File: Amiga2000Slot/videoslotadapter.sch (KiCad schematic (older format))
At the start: 20 parts, among them U1 74LVC86, U2 74LVC574, U3 74LVC574, U4 TLV74333PDBVR, U5 74LVC86

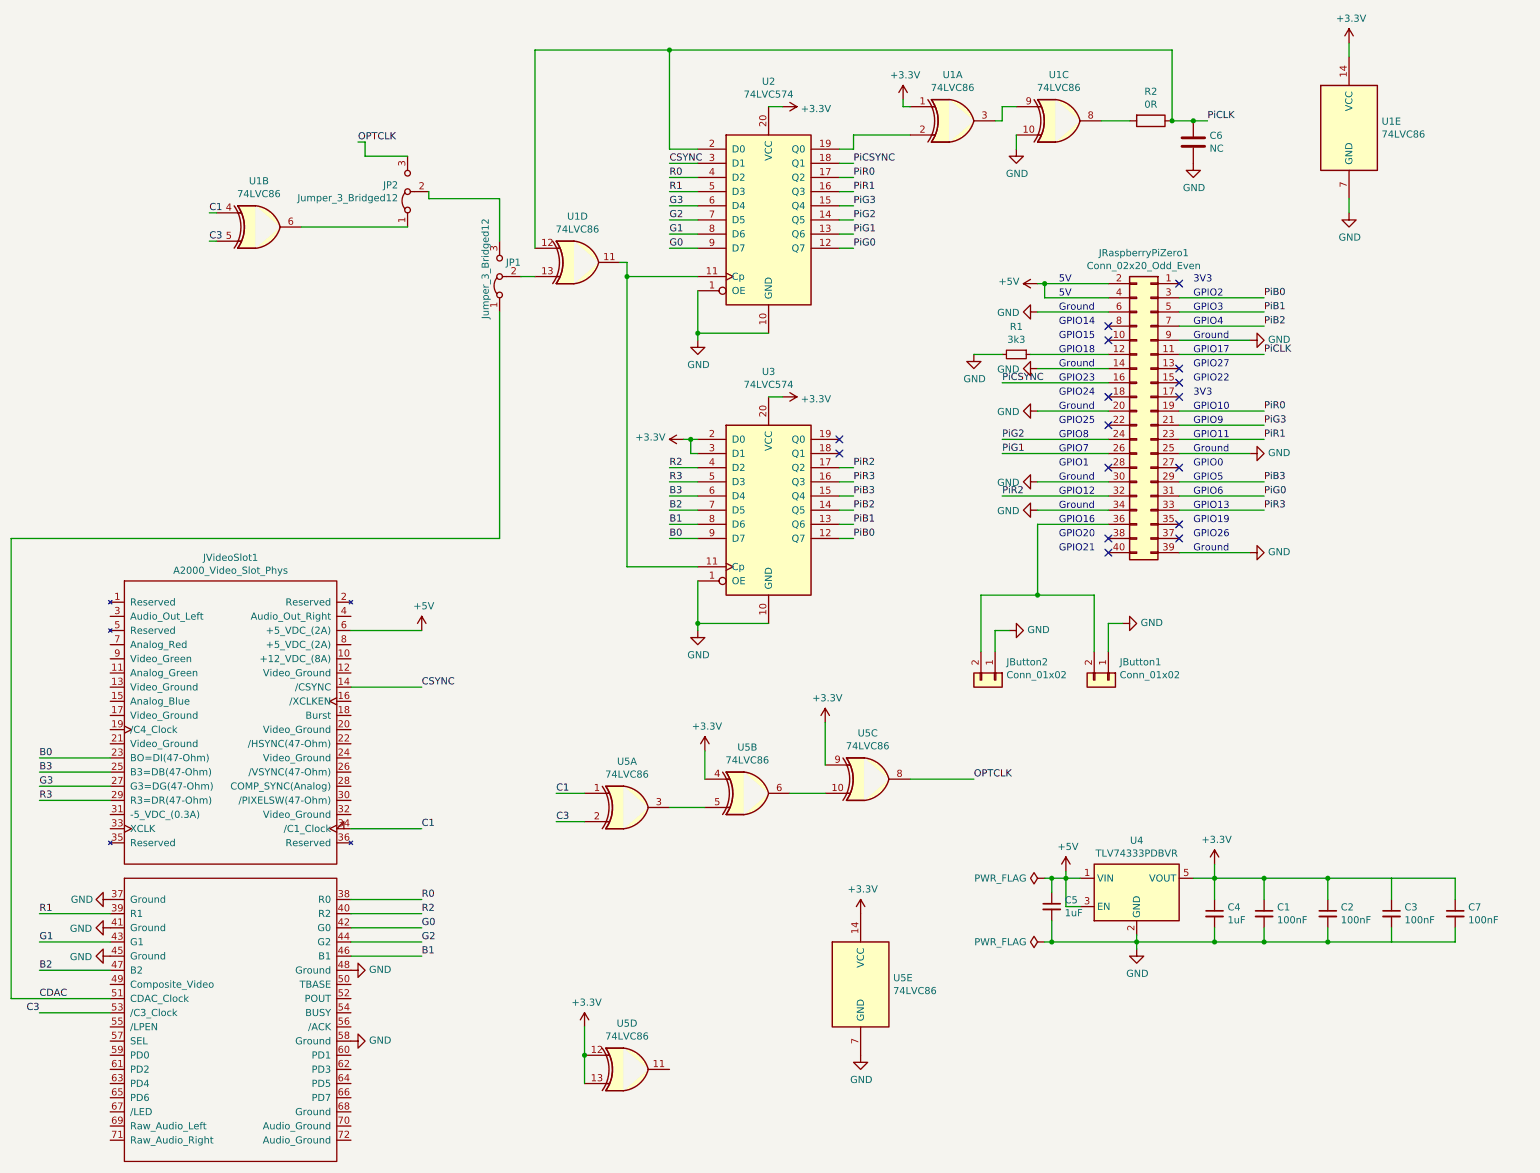
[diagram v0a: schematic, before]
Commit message: A2000SlotV3 initial dump
* Strip out most of the options since we have a pretty stable build now.
* Add the mounting holes to the schematic and use M3s (need to check
  positioning later)

Note: At this stage this has not been built and there may be dragons.
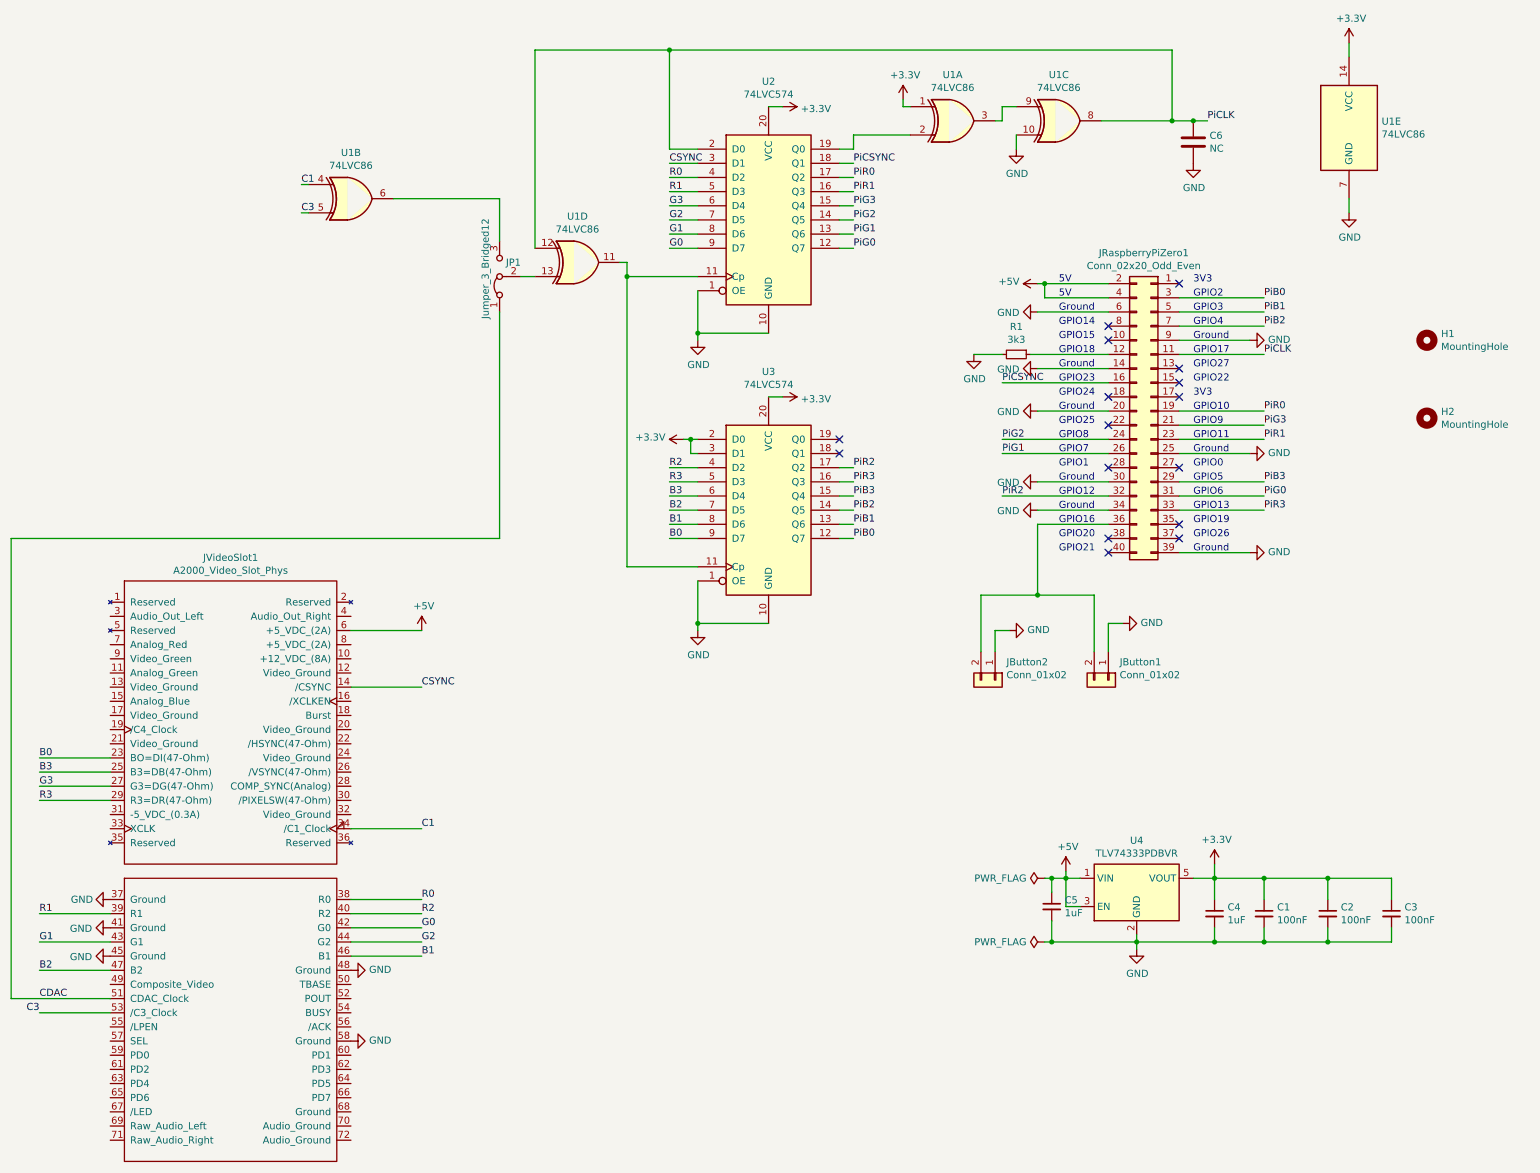
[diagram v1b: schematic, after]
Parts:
- removed C7: 100nF, Capacitor_SMD:C_0603_1608Metric_Pad1.08x0.95mm_HandSolder, symbol Device:C_Small
- removed JP2: Jumper_3_Bridged12, Jumper:SolderJumper-3_P1.3mm_Open_Pad1.0x1.5mm, symbol Jumper:Jumper_3_Bridged12
- removed R2: 0R, Resistor_SMD:R_0603_1608Metric_Pad0.98x0.95mm_HandSolder, symbol Device:R
- removed U5: 74LVC86, Package_SO:TSSOP-14_4.4x5mm_P0.65mm, symbol 74xx:74HC86
- added H1, H2: MountingHole, MountingHole:MountingHole_3.2mm_M3_ISO14580, symbol Mechanical:MountingHole
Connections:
- net PiCLK: now also U1.8
- net at U1.6: now also JP1.3 (B)
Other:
- moved on the sheet: U1B
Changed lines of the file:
@@
 	4500 2350 4500 2050
 Wire Wire Line
-	2450 2150 2500 2150
+	3100 1950 3150 1950
 $Comp
 L Jumper:Jumper_3_Bridged12 JP1
@@
 Wire Wire Line
 	8400 7300 9000 7300
-Text Label 2450 2150 0    50   ~ 0
+Text Label 3100 1950 0    50   ~ 0
 C1
-Text Label 2450 2350 0    50   ~ 0
+Text Label 3100 2150 0    50   ~ 0
 C3
 Wire Wire Line
-	2450 2350 2500 2350
+	3100 2150 3150 2150
 $Comp
 L power:GND #PWR0110
@@
 	0    1    1    0
 $EndComp
-$Comp
-L Device:R R2
-U 1 1 6050C725
-P 9100 1500
-F 0 "R2" V 8893 1500 50  0000 C CNN
-F 1 "0R" V 8984 1500 50  0000 C CNN
-F 2 "Resistor_SMD:R_0603_1608Metric_Pad0.98x0.95mm_HandSolder" V 9030 1500 50  0001 C CNN
-F 3 "~" H 9100 1500 50  0001 C CNN
-	1    9100 1500
-	0    1    1    0
-$EndComp
-Wire Wire Line
-	8950 1500 8750 1500
 Wire Wire Line
 	9250 1000 9250 1500
@@
 Wire Wire Line
 	9250 1500 9400 1500
-Connection ~ 9250 1500
 $Comp
 L Device:C C6
@@
 $EndComp
 $Comp
-L 74xx:74HC86 U5
-U 1 1 605761FE
-P 5400 6350
-F 0 "U5" H 5400 6675 50  0000 C CNN
-F 1 "74LVC86" H 5400 6584 50  0000 C CNN
-F 2 "Package_SO:TSSOP-14_4.4x5mm_P0.65mm" H 5400 6350 50  0001 C CNN
-F 3 "http://www.ti.com/lit/gpn/sn74HC86" H 5400 6350 50  0001 C CNN
-	1    5400 6350
-	1    0    0    -1
-$EndComp
-$Comp
-L 74xx:74HC86 U5
-U 2 1 60577A87
-P 6250 6250
-F 0 "U5" H 6250 6575 50  0000 C CNN
-F 1 "74LVC86" H 6250 6484 50  0000 C CNN
-F 2 "Package_SO:TSSOP-14_4.4x5mm_P0.65mm" H 6250 6250 50  0001 C CNN
-F 3 "http://www.ti.com/lit/gpn/sn74HC86" H 6250 6250 50  0001 C CNN
-	2    6250 6250
-	1    0    0    -1
-$EndComp
-$Comp
-L 74xx:74HC86 U5
-U 3 1 60579173
-P 7100 6150
-F 0 "U5" H 7100 6475 50  0000 C CNN
-F 1 "74LVC86" H 7100 6384 50  0000 C CNN
-F 2 "Package_SO:TSSOP-14_4.4x5mm_P0.65mm" H 7100 6150 50  0001 C CNN
-F 3 "http://www.ti.com/lit/gpn/sn74HC86" H 7100 6150 50  0001 C CNN
-	3    7100 6150
-	1    0    0    -1
-$EndComp
-$Comp
-L 74xx:74HC86 U5
-U 4 1 6057ADAC
-P 5400 8200
-F 0 "U5" H 5400 8525 50  0000 C CNN
-F 1 "74LVC86" H 5400 8434 50  0000 C CNN
-F 2 "Package_SO:TSSOP-14_4.4x5mm_P0.65mm" H 5400 8200 50  0001 C CNN
-F 3 "http://www.ti.com/lit/gpn/sn74HC86" H 5400 8200 50  0001 C CNN
-	4    5400 8200
-	1    0    0    -1
-$EndComp
-$Comp
-L 74xx:74HC86 U5
-U 5 1 6057C8D9
-P 7050 7600
-F 0 "U5" H 7280 7646 50  0000 L CNN
-F 1 "74LVC86" H 7280 7555 50  0000 L CNN
-F 2 "Package_SO:TSSOP-14_4.4x5mm_P0.65mm" H 7050 7600 50  0001 C CNN
-F 3 "http://www.ti.com/lit/gpn/sn74HC86" H 7050 7600 50  0001 C CNN
-	5    7050 7600
-	1    0    0    -1
-$EndComp
-$Comp
-L power:GND #PWR0132
-U 1 1 6057E0A6
-P 7050 8100
-F 0 "#PWR0132" H 7050 7850 50  0001 C CNN
-F 1 "GND" H 7055 7927 50  0000 C CNN
-F 2 "" H 7050 8100 50  0001 C CNN
-F 3 "" H 7050 8100 50  0001 C CNN
-	1    7050 8100
-	1    0    0    -1
-$EndComp
-$Comp
-L power:+3.3V #PWR0133
-U 1 1 6057F572
-P 7050 7100
-F 0 "#PWR0133" H 7050 6950 50  0001 C CNN
-F 1 "+3.3V" H 7065 7273 50  0000 C CNN
-F 2 "" H 7050 7100 50  0001 C CNN
-F 3 "" H 7050 7100 50  0001 C CNN
-	1    7050 7100
-	1    0    0    -1
-$EndComp
-Text Label 4900 6250 0    50   ~ 0
-C1
-Text Label 4900 6450 0    50   ~ 0
-C3
-Wire Wire Line
-	5100 6250 4900 6250
-Wire Wire Line
-	4900 6450 5100 6450
-Wire Wire Line
-	5950 6350 5700 6350
-$Comp
-L power:+3.3V #PWR0134
-U 1 1 605AC462
-P 5950 5950
-F 0 "#PWR0134" H 5950 5800 50  0001 C CNN
-F 1 "+3.3V" H 5965 6123 50  0000 C CNN
-F 2 "" H 5950 5950 50  0001 C CNN
-F 3 "" H 5950 5950 50  0001 C CNN
-	1    5950 5950
-	1    0    0    -1
-$EndComp
-Wire Wire Line
-	5950 5950 5950 6150
-Wire Wire Line
-	6800 6250 6550 6250
-$Comp
-L power:+3.3V #PWR0135
-U 1 1 605CB272
-P 6800 5750
-F 0 "#PWR0135" H 6800 5600 50  0001 C CNN
-F 1 "+3.3V" H 6815 5923 50  0000 C CNN
-F 2 "" H 6800 5750 50  0001 C CNN
-F 3 "" H 6800 5750 50  0001 C CNN
-	1    6800 5750
-	1    0    0    -1
-$EndComp
-Wire Wire Line
-	6800 5750 6800 6050
-Wire Wire Line
-	7400 6150 7850 6150
-Text Label 7850 6150 0    50   ~ 0
-OPTCLK
-$Comp
-L power:+3.3V #PWR0136
-U 1 1 605E14F4
-P 5100 7900
-F 0 "#PWR0136" H 5100 7750 50  0001 C CNN
-F 1 "+3.3V" H 5115 8073 50  0000 C CNN
-F 2 "" H 5100 7900 50  0001 C CNN
-F 3 "" H 5100 7900 50  0001 C CNN
-	1    5100 7900
-	1    0    0    -1
-$EndComp
-Wire Wire Line
-	5100 7900 5100 8100
-Wire Wire Line
-	5100 8300 5100 8100
-Connection ~ 5100 8100
-$Comp
-L Jumper:Jumper_3_Bridged12 JP2
-U 1 1 60611B79
-P 3850 2000
-F 0 "JP2" V 3896 2067 50  0000 L CNN
-F 1 "Jumper_3_Bridged12" V 3805 2067 50  0000 L CNN
-F 2 "Jumper:SolderJumper-3_P1.3mm_Open_Pad1.0x1.5mm" H 3850 2000 50  0001 C CNN
-F 3 "~" H 3850 2000 50  0001 C CNN
-	1    3850 2000
-	0    -1   -1   0
-$EndComp
-$Comp
 L 74xx:74HC86 U1
 U 2 1 5F5643BE
-P 2800 2250
-F 0 "U1" H 2800 2575 50  0000 C CNN
-F 1 "74LVC86" H 2800 2484 50  0000 C CNN
-F 2 "Package_SO:TSSOP-14_4.4x5mm_P0.65mm" H 2800 2250 50  0001 C CNN
-F 3 "http://www.ti.com/lit/gpn/sn74HC86" H 2800 2250 50  0001 C CNN
-	2    2800 2250
-	1    0    0    -1
-$EndComp
-Wire Wire Line
-	3100 2250 3850 2250
-Wire Wire Line
-	3850 1750 3550 1750
-Wire Wire Line
-	3550 1750 3550 1650
-Wire Wire Line
-	3550 1650 3500 1650
-Text Label 3500 1650 0    50   ~ 0
-OPTCLK
-Wire Wire Line
-	4500 2050 4000 2050
-Wire Wire Line
-	4000 2050 4000 2000
-$Comp
-L Device:C_Small C7
-U 1 1 606779AE
-P 11250 7100
-F 0 "C7" H 11342 7146 50  0000 L CNN
-F 1 "100nF" H 11342 7055 50  0000 L CNN
-F 2 "Capacitor_SMD:C_0603_1608Metric_Pad1.08x0.95mm_HandSolder" H 11250 7100 50  0001 C CNN
-F 3 "~" H 11250 7100 50  0001 C CNN
-	1    11250 7100
-	1    0    0    -1
-$EndComp
-Wire Wire Line
-	10800 6850 11250 6850
-Wire Wire Line
-	11250 6850 11250 7000
-Wire Wire Line
-	11250 7200 11250 7300
-Wire Wire Line
-	11250 7300 10800 7300
+P 3450 2050
+F 0 "U1" H 3450 2375 50  0000 C CNN
+F 1 "74LVC86" H 3450 2284 50  0000 C CNN
+F 2 "Package_SO:TSSOP-14_4.4x5mm_P0.65mm" H 3450 2050 50  0001 C CNN
+F 3 "http://www.ti.com/lit/gpn/sn74HC86" H 3450 2050 50  0001 C CNN
+	2    3450 2050
+	1    0    0    -1
+$EndComp
+Wire Wire Line
+	3750 2050 4500 2050
+Wire Wire Line
+	8750 1500 9250 1500
+Connection ~ 9250 1500
+$Comp
+L Mechanical:MountingHole H1
+U 1 1 60706178
+P 11050 3050
+F 0 "H1" H 11150 3096 50  0000 L CNN
+F 1 "MountingHole" H 11150 3005 50  0000 L CNN
+F 2 "MountingHole:MountingHole_3.2mm_M3_ISO14580" H 11050 3050 50  0001 C CNN
+F 3 "~" H 11050 3050 50  0001 C CNN
+	1    11050 3050
+	1    0    0    -1
+$EndComp
+$Comp
+L Mechanical:MountingHole H2
+U 1 1 60706E1A
+P 11050 3600
+F 0 "H2" H 11150 3646 50  0000 L CNN
+F 1 "MountingHole" H 11150 3555 50  0000 L CNN
+F 2 "MountingHole:MountingHole_3.2mm_M3_ISO14580" H 11050 3600 50  0001 C CNN
+F 3 "~" H 11050 3600 50  0001 C CNN
+	1    11050 3600
+	1    0    0    -1
+$EndComp
 $EndSCHEMATC
